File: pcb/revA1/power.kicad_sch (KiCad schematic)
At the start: 24 parts, among them J5 5V_PRG, U13 1117-3.3, U14 1117-3.3, U15 1117-1.2

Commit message: revA1, WIP
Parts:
- C42: renamed from C41; footprint Capacitor_SMD:CP_Elec_6.3x7.7 -> Capacitor_Tantalum_SMD:CP_EIA-6032-28_Kemet-C_HandSolder
- J6: renamed from J5; value 5V_PRG -> PRG
- renumbered C40 to C41, C42 to C43, C43 to C44, C44 to C45, C45 to C46, C46 to C47, C47 to C48, C48 to C49, C49 to C50, C50 to C51, C51 to C52, C52 to C53, C53 to C54, C54 to C55, C55 to C56, R27 to R30, R28 to R31, R29 to R32, U13 to U15, U14 to U16, U15 to U17

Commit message: Small improvements to the revA1
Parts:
- J6: now not fitted
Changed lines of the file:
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@@
 	(title_block
 		(title "Karabas-MegaBuzz")
-		(date "2026-05-27")
+		(date "2026-05-29")
 		(rev "A1")
 		(company "Andy Karpov")
@@
 		(on_board yes)
 		(in_pos_files yes)
-		(dnp no)
+		(dnp yes)
 		(fields_autoplaced yes)
 		(property "Reference" "J6"

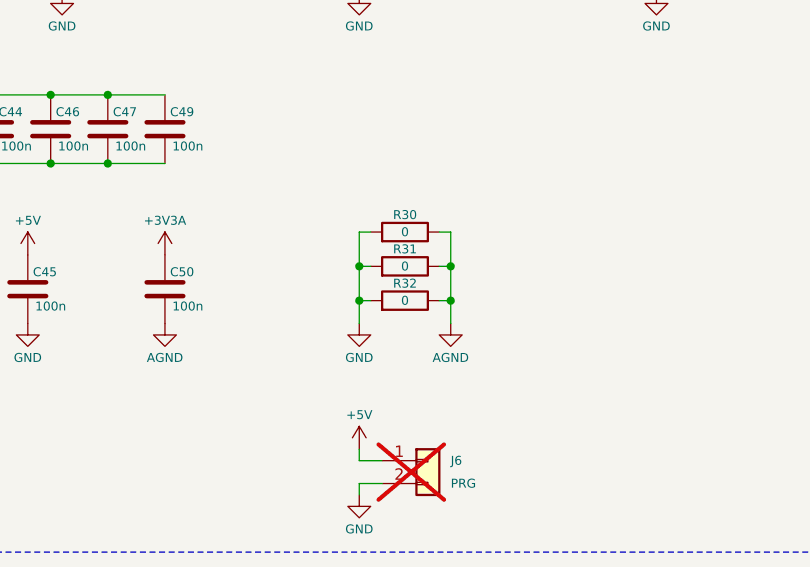
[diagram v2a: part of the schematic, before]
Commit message: Fixed missing LED1 connection, new revA1 release
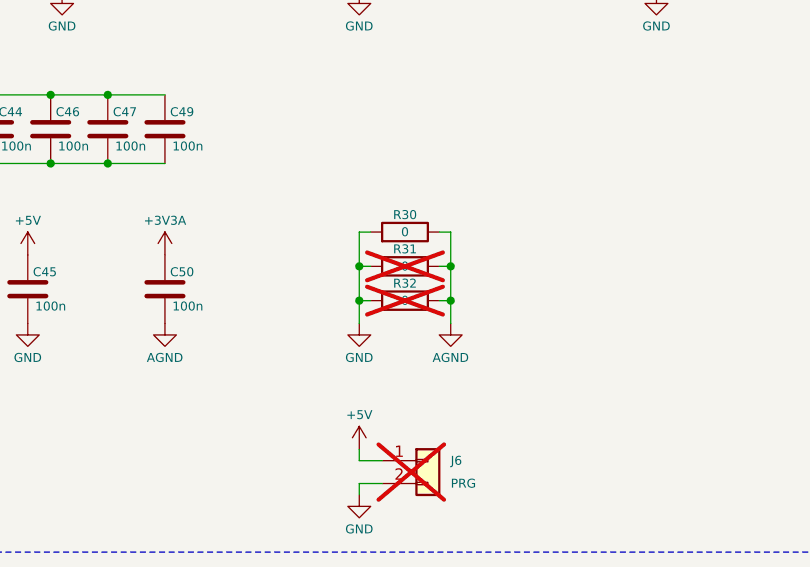
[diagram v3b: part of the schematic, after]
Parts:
- R31, R32: now not fitted; now left out of the parts list
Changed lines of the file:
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@@
 		(body_style 1)
 		(exclude_from_sim no)
-		(in_bom yes)
-		(on_board yes)
-		(in_pos_files yes)
-		(dnp no)
+		(in_bom no)
+		(on_board yes)
+		(in_pos_files yes)
+		(dnp yes)
 		(property "Reference" "R31"
 			(at 81.28 74.295 90)
@@
 		(body_style 1)
 		(exclude_from_sim no)
-		(in_bom yes)
-		(on_board yes)
-		(in_pos_files yes)
-		(dnp no)
+		(in_bom no)
+		(on_board yes)
+		(in_pos_files yes)
+		(dnp yes)
 		(property "Reference" "R32"
 			(at 81.28 78.105 90)
